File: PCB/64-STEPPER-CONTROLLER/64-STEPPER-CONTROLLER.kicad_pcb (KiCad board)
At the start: 2 copper layers, 118.7 x 99.7 mm, 5 parts, among them J1 IPS1-125-01-S-D, J2 IPS1-125-01-S-D, U1 Teensy4.0, U2 Teensy4.1, U3 Teensy4.0

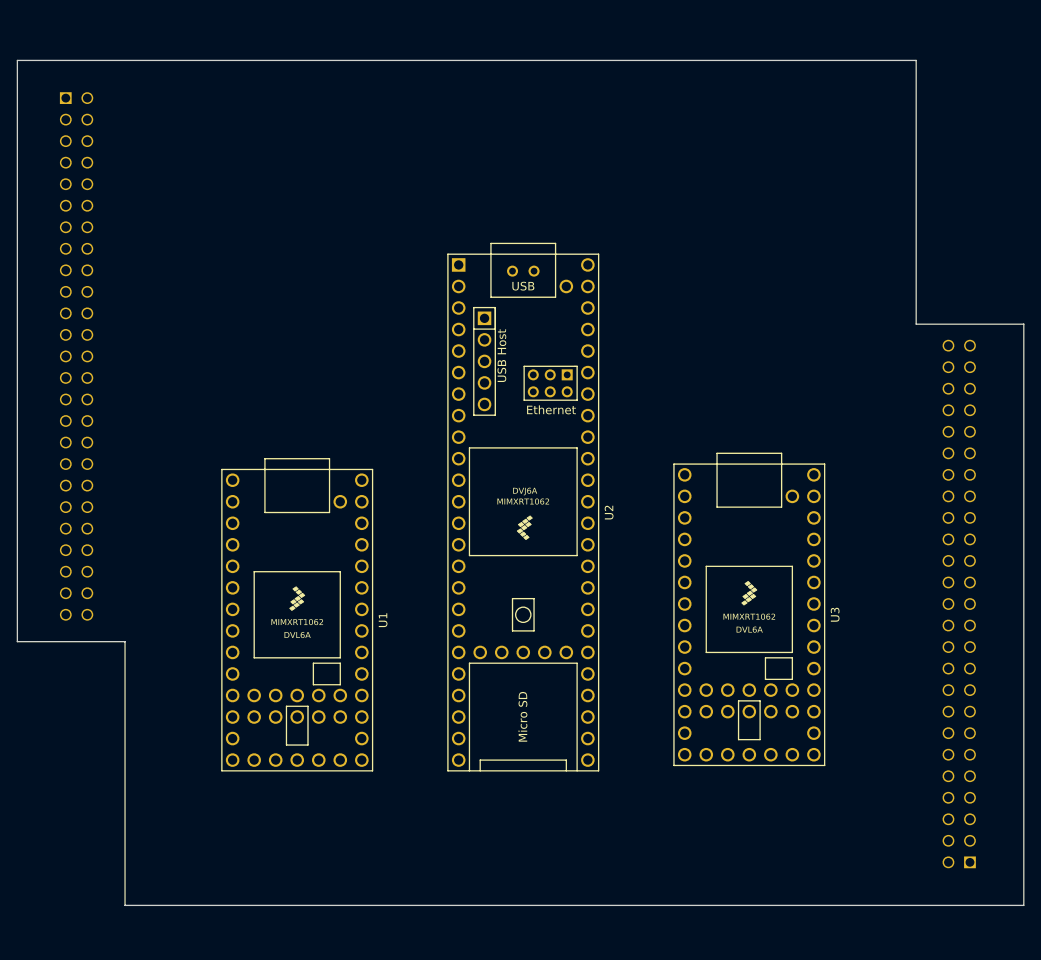
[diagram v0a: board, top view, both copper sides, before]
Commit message: Finish design of main board
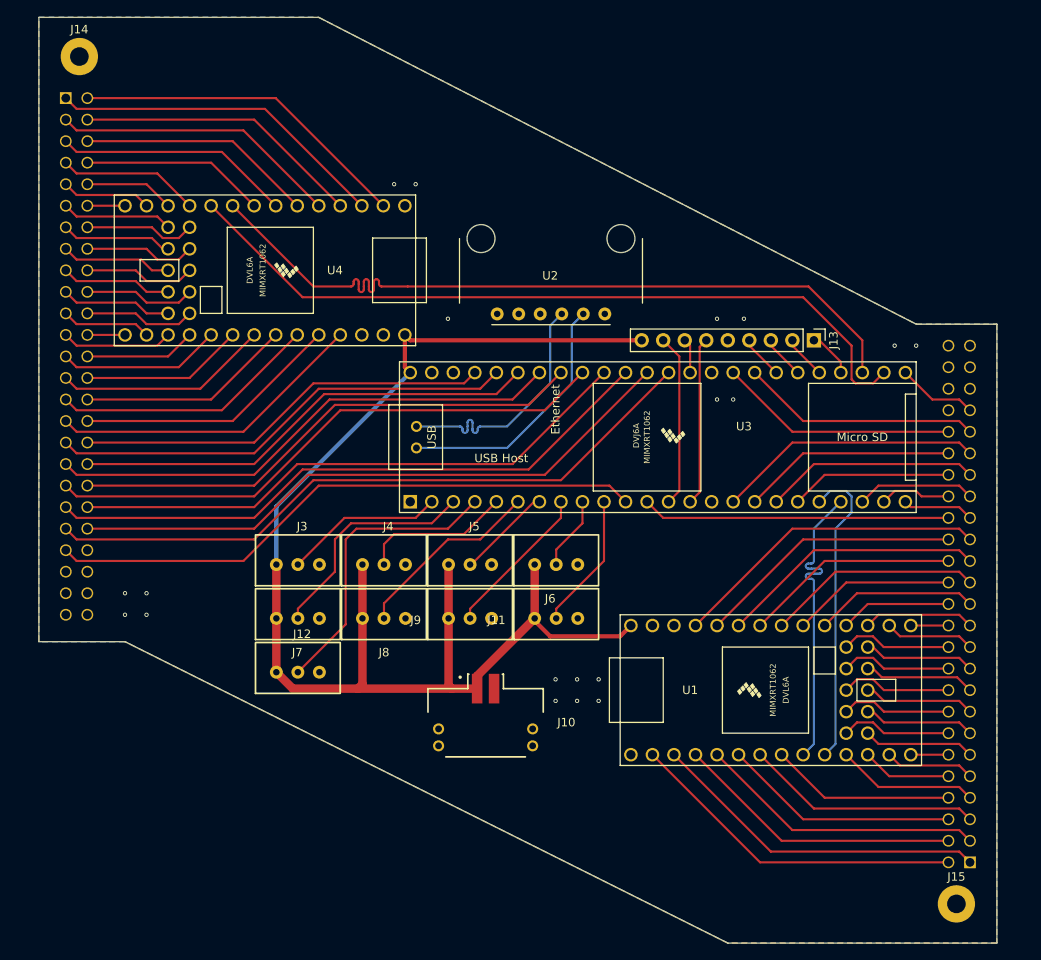
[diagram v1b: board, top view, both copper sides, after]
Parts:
- added J10: UMPT-02-01-X-RA-WT-P-X, REFERENCES:SAMTEC_UMPT-02-01-X-RA-WT-P-X, F.Cu at (142.9, 115.4)
- added J11: Conn_01x03, REFERENCES:3-PIN TERMINAL, F.Cu at (146.2, 103.9)
- added J12: Conn_01x03, REFERENCES:3-PIN TERMINAL, F.Cu at (115.7, 110.2)
- added J13: Conn_01x09, Connector_PinHeader_2.54mm:PinHeader_1x09_P2.54mm_Vertical, F.Cu at (181.6, 68.6)
- added J14: Screw_Terminal_01x01, MountingHole:MountingHole_2.2mm_M2_Pad, F.Cu at (94.9, 35.1)
- added J15: Screw_Terminal_01x01, MountingHole:MountingHole_2.2mm_M2_Pad, F.Cu at (198.4, 135.1)
- added J3: Conn_01x03, REFERENCES:3-PIN TERMINAL, F.Cu at (115.7, 97.5)
- added J4: Conn_01x03, REFERENCES:3-PIN TERMINAL, F.Cu at (125.9, 97.5)
- added J5: Conn_01x03, REFERENCES:3-PIN TERMINAL, F.Cu at (136.0, 97.5)
- added J6: Conn_01x03, REFERENCES:3-PIN TERMINAL, F.Cu at (146.2, 97.5)
- added J7: Conn_01x03, REFERENCES:3-PIN TERMINAL, F.Cu at (115.7, 103.9)
- added J8: Conn_01x03, REFERENCES:3-PIN TERMINAL, F.Cu at (125.9, 103.9)
- added J9: Conn_01x03, REFERENCES:3-PIN TERMINAL, F.Cu at (136.0, 103.9)
- added U4: Teensy4.0, REFERENCES:Teensy40, F.Cu at (116.8, 60.3)
- J1, J2: footprint LIBRARIES:SAMTEC_IPS1-125-01-S-D -> REFERENCES:SAMTEC_IPS1-125-01-S-D
- U1: footprint LIBRARIES:Teensy40 -> REFERENCES:Teensy40
- U2: value Teensy4.1 -> USB-C_Module; footprint LIBRARIES:Teensy41 -> REFERENCES:USB-C-MODULE
- U3: value Teensy4.0 -> Teensy4.1; footprint LIBRARIES:Teensy40 -> REFERENCES:Teensy41
- moved U1 56.5 mm to (176.5, 109.9), turned to 0 degrees
- moved U3 23.6 mm to (163.2, 80.0), turned to 0 degrees
- moved U2 23.4 mm to (139.8, 66.7), turned to 0 degrees
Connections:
- J1 pad 44: VCC -> unconnected-(J1-Pad44)
- J1 pad 45: +5V -> unconnected-(J1-Pad45)
- J1 pad 46: +5V -> unconnected-(J1-Pad46)
- J2 pad 44: VCC -> unconnected-(J2-Pad44)
- J2 pad 45: +5V -> unconnected-(J2-Pad45)
- J2 pad 46: +5V -> unconnected-(J2-Pad46)
- U1 pad 10: unconnected-(U1-Pad10) -> RX1
- U1 pad 11: unconnected-(U1-Pad11) -> 1A5STEP
- U1 pad 12: unconnected-(U1-Pad12) -> 2A4STEP
- U1 pad 13: unconnected-(U1-Pad13) -> 2A8STEP
- U1 pad 14: unconnected-(U1-Pad14) -> 2A3STEP
- U1 pad 2: unconnected-(U1-Pad2) -> 1A4STEP
- U1 pad 20: unconnected-(U1-Pad20) -> 3A1STEP
- U1 pad 21: unconnected-(U1-Pad21) -> 3A6STEP
- U1 pad 22: unconnected-(U1-Pad22) -> 3A5STEP
- U1 pad 23: unconnected-(U1-Pad23) -> 4A4STEP
- U1 pad 24: unconnected-(U1-Pad24) -> 4A8STEP
- U1 pad 25: unconnected-(U1-Pad25) -> 4A3STEP
- U1 pad 26: unconnected-(U1-Pad26) -> 4A7STEP
- U1 pad 27: unconnected-(U1-Pad27) -> 4A2STEP
- U1 pad 28: unconnected-(U1-Pad28) -> 4A6STEP
- U1 pad 29: unconnected-(U1-Pad29) -> 4A1STEP
- U1 pad 3: unconnected-(U1-Pad3) -> 1A8STEP
- U1 pad 30: unconnected-(U1-Pad30) -> 4A5STEP
- U1 pad 33: unconnected-(U1-Pad33) -> +5V
- U1 pad 35: unconnected-(U1-Pad35) -> 3A7STEP
- U1 pad 36: unconnected-(U1-Pad36) -> 3A2STEP
- U1 pad 37: unconnected-(U1-Pad37) -> 3A8STEP
- U1 pad 38: unconnected-(U1-Pad38) -> 3A3STEP
- U1 pad 39: unconnected-(U1-Pad39) -> 2A5STEP
- U1 pad 4: unconnected-(U1-Pad4) -> 1A3STEP
- U1 pad 40: unconnected-(U1-Pad40) -> 3A4STEP
- U1 pad 41: unconnected-(U1-Pad41) -> 2A6STEP
- U1 pad 42: unconnected-(U1-Pad42) -> 2A1STEP
- U1 pad 43: unconnected-(U1-Pad43) -> 2A7STEP
- U1 pad 44: unconnected-(U1-Pad44) -> 2A2STEP
- U1 pad 5: unconnected-(U1-Pad5) -> 1A7STEP
- U1 pad 6: unconnected-(U1-Pad6) -> 1A2STEP
- U1 pad 7: unconnected-(U1-Pad7) -> 1A6STEP
- U1 pad 8: unconnected-(U1-Pad8) -> 1A1STEP
- U1 pad 9: unconnected-(U1-Pad9) -> TX1
- U2 pad 1: GND -> unconnected-(U2-Pad1)
- U2 pad 2: unconnected-(U2-Pad2) -> GND
- U2 pad 4: unconnected-(U2-Pad4) -> D-
- U2 pad 5: unconnected-(U2-Pad5) -> D+
- U3 pad 10: unconnected-(U3-Pad10) -> LED8
- U3 pad 11: unconnected-(U3-Pad11) -> SER8
- U3 pad 12: unconnected-(U3-Pad12) -> SER1
- U3 pad 13: unconnected-(U3-Pad13) -> MOSI
- U3 pad 14: unconnected-(U3-Pad14) -> MISO
- U3 pad 16: unconnected-(U3-Pad16) -> SER2
- U3 pad 17: GND -> SRCLK3
- U3 pad 18: unconnected-(U3-Pad18) -> RCLK1
- U3 pad 19: unconnected-(U3-Pad19) -> ~{OE1}
- U3 pad 2: unconnected-(U3-Pad2) -> LED1
- U3 pad 20: unconnected-(U3-Pad20) -> RX1
- U3 pad 21: unconnected-(U3-Pad21) -> TX1
- U3 pad 22: unconnected-(U3-Pad22) -> ~{SRCLR1}
- U3 pad 23: unconnected-(U3-Pad23) -> SRCLK2
- U3 pad 24: unconnected-(U3-Pad24) -> SRCLK1
- U3 pad 25: unconnected-(U3-Pad25) -> SER4
- U3 pad 26: unconnected-(U3-Pad26) -> RX2
- U3 pad 27: unconnected-(U3-Pad27) -> TX2
- U3 pad 28: unconnected-(U3-Pad28) -> CS2
- U3 pad 29: unconnected-(U3-Pad29) -> CS1
- U3 pad 3: unconnected-(U3-Pad3) -> LED5
- U3 pad 30: unconnected-(U3-Pad30) -> DC
- U3 pad 31: unconnected-(U3-Pad31) -> RST
- U3 pad 32: GND -> SER3
- U3 pad 33: unconnected-(U3-Pad33) -> SRCLK4
- U3 pad 34: unconnected-(U3-Pad34) -> GND
- U3 pad 35: unconnected-(U3-Pad35) -> SCK
- U3 pad 36: unconnected-(U3-Pad36) -> SER7
- U3 pad 37: unconnected-(U3-Pad37) -> SRCLK8
- U3 pad 38: unconnected-(U3-Pad38) -> SER6
- U3 pad 39: unconnected-(U3-Pad39) -> SRCLK7
- U3 pad 4: unconnected-(U3-Pad4) -> LED9
- U3 pad 40: unconnected-(U3-Pad40) -> RCLK2
- U3 pad 41: unconnected-(U3-Pad41) -> ~{OE2}
- U3 pad 42: unconnected-(U3-Pad42) -> ~{SRCLR2}
- U3 pad 43: unconnected-(U3-Pad43) -> SRCLK6
- U3 pad 44: unconnected-(U3-Pad44) -> SRCLK5
- U3 pad 5: unconnected-(U3-Pad5) -> LED2
- U3 pad 6: unconnected-(U3-Pad6) -> LED6
- U3 pad 7: unconnected-(U3-Pad7) -> LED3
- U3 pad 8: unconnected-(U3-Pad8) -> LED7
- U3 pad 9: unconnected-(U3-Pad9) -> LED4
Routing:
- net +5V: track 0.00 -> 159.3 mm
- net RX2: track 0.00 -> 90.9 mm
- net TX2: track 0.00 -> 90.8 mm
- net SER7: track 0.00 -> 79.8 mm
- net SRCLK8: track 0.00 -> 73.7 mm
- net SER6: track 0.00 -> 73.7 mm
- net SER8: track 0.00 -> 71.0 mm
- net RCLK2: track 0.00 -> 67.5 mm
- net SRCLK7: track 0.00 -> 67.5 mm
- net ~{SRCLR2}: track 0.00 -> 61.4 mm
- net ~{OE2}: track 0.00 -> 61.4 mm
- net SRCLK5: track 0.00 -> 55.3 mm
- net SRCLK6: track 0.00 -> 55.3 mm
- net SER5: track 0.00 -> 49.1 mm
- net 1A8STEP: track 0.00 -> 40.2 mm
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- added copper zone on B.Cu, net GND
- added copper zone on F.Cu, net GND
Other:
- board size 118.7 x 99.7 mm -> 113 x 109.2 mm

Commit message: final changes to 64-pcb and testing renders
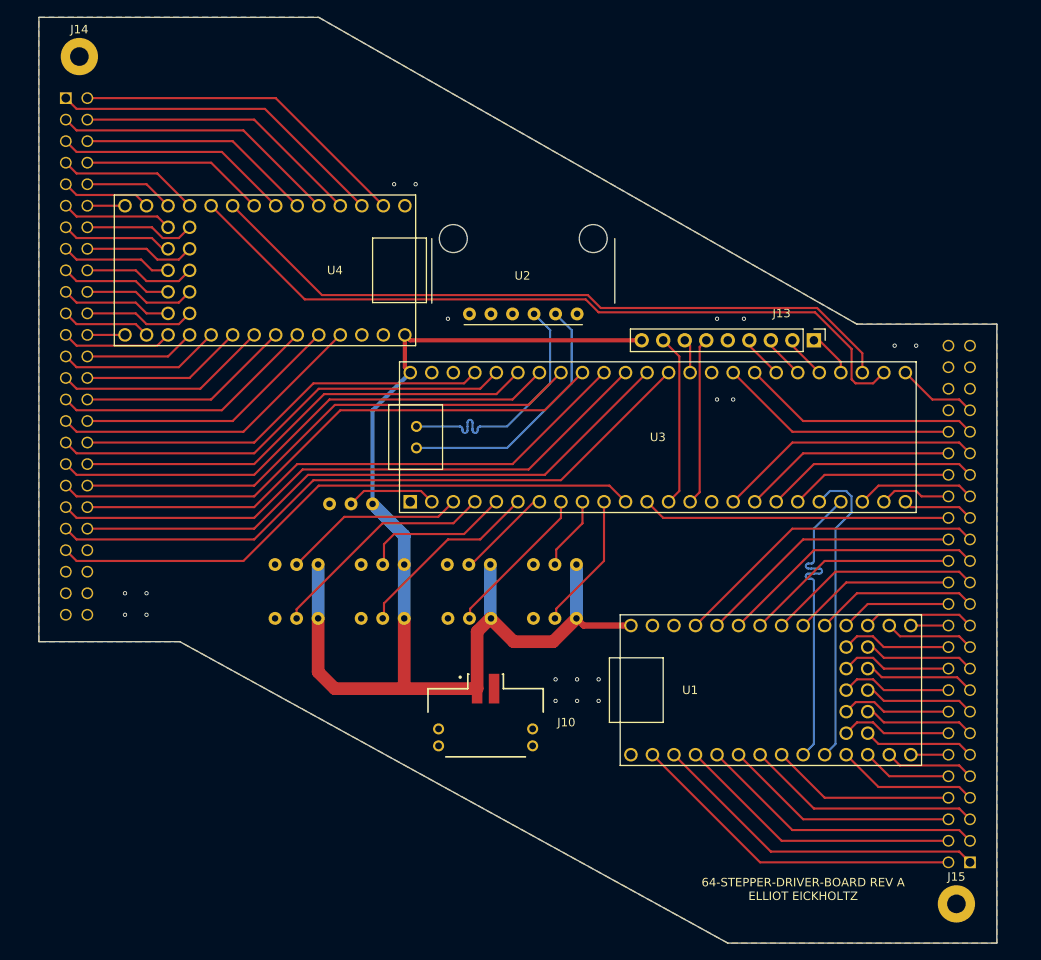
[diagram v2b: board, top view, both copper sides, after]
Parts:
- J11, J12, J3, J4, J5, J6, J7, J8, J9: moved to B.Cu
- moved J12 25.7 mm to (132.0, 90.4), turned to 180 degrees
- moved J9 9.93 mm to (146.0, 103.9), turned to 180 degrees
- moved J5 9.85 mm to (145.9, 97.5), turned to 180 degrees
- moved J3 9.85 mm to (125.6, 97.5), turned to 180 degrees
- moved J4 9.85 mm to (135.7, 97.5), turned to 180 degrees
- moved J7 9.85 mm to (125.6, 103.9), turned to 180 degrees
- moved J8 9.85 mm to (135.7, 103.9), turned to 180 degrees
- moved J11 9.85 mm to (156.1, 103.9), turned to 180 degrees
- moved J6 9.85 mm to (156.1, 97.5), turned to 180 degrees
- moved U2 3.27 mm to (136.5, 66.7)
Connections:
- J12 pad 2: LED9 -> LED1
- J3 pad 2: LED1 -> LED5
- J7 pad 2: LED5 -> LED9
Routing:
- net +5V: track 159.3 -> 146.8 mm
- net LED1: track 18.9 -> 10.7 mm
- net LED9: track 35.1 -> 27.4 mm
- net TX2: track 90.8 -> 83.8 mm
- net LED5: track 26.9 -> 21.6 mm
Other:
- outline, holes or cut-outs redrawn
- board text added: "64-STEPPER-DRIVER-BOARD REV A ELLIOT EICKHOLTZ"
